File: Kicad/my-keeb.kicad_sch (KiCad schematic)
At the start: 262 parts, among them SW10 SW_Push, SW11 SW_Push, SW12 SW_Push, SW13 SW_Push, SW14 SW_Push, SW15 SW_Push, SW16 SW_Push, SW17 SW_Push, SW18 SW_Push, SW19 SW_Push, SW2 SW_Push, SW20 SW_Push, SW21 SW_Push, SW22 SW_Push, SW23 SW_Push, SW24 SW_Push, SW25 SW_Push, SW26 SW_Push, SW27 SW_Push, SW29 SW_Push, SW3 SW_Push, SW30 SW_Push, SW31 SW_Push, SW32 SW_Push, SW33 SW_Push, SW34 SW_Push, SW35 SW_Push, SW36 SW_Push, SW37 SW_Push, SW38 SW_Push, SW39 SW_Push, SW4 SW_Push, SW40 SW_Push, SW41 SW_Push, SW42 SW_Push, SW43 SW_Push, SW44 SW_Push, SW45 SW_Push, SW46 SW_Push, SW47 SW_Push, SW48 SW_Push, SW49 SW_Push, SW5 SW_Push, SW50 SW_Push, SW51 SW_Push, SW52 SW_Push, SW53 SW_Push, SW54 SW_Push, SW55 SW_Push, SW57 SW_Push, SW58 SW_Push, SW6 SW_Push, SW60 SW_Push, SW61 SW_Push, SW62 SW_Push, SW63 SW_Push, SW64 SW_Push, SW65 SW_Push, SW66 SW_Push, SW67 SW_Push, SW68 SW_Push, SW69 SW_Push, SW7 SW_Push, SW71 SW_Push, SW72 SW_Push, SW73 SW_Push, SW74 SW_Push, SW77 SW_Push, SW79 SW_Push, SW8 SW_Push, SW80 SW_Push, SW81 SW_Push, SW82 SW_Push, SW86 SW_Push, SW87 SW_Push, SW88 SW_Push, SW89 SW_Push, SW9 SW_Push, SW90 SW_Push, SW91 SW_Push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

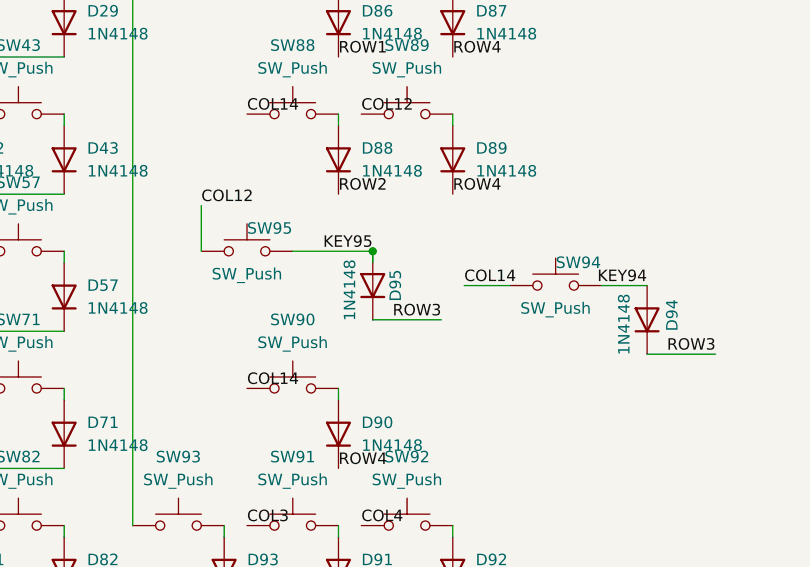
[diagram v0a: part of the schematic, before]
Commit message: Organize files into folders
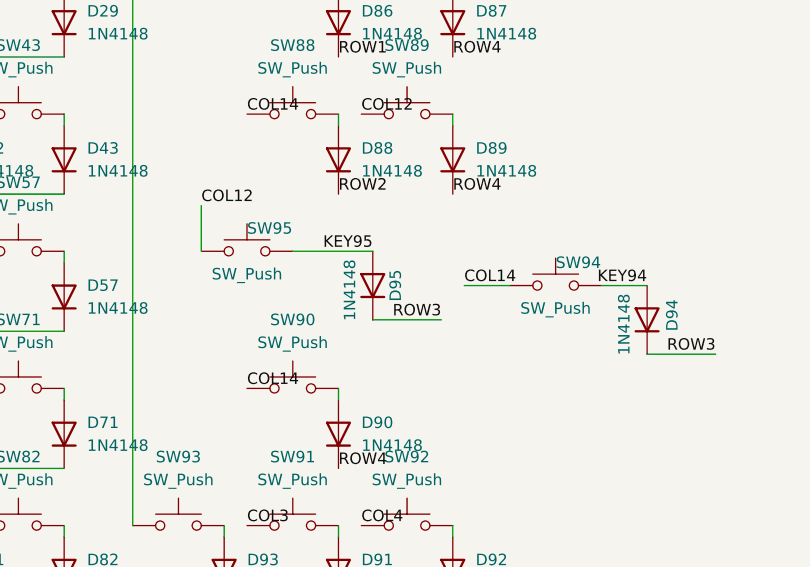
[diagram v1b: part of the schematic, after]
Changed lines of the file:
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@@
 	)
 	(junction
-		(at 243.84 68.58)
-		(diameter 0)
-		(color 0 0 0 0)
-	)
-	(junction
 		(at 44.45 77.47)
 		(diameter 0)
@@
 	(wire
 		(pts
-			(xy 251.46 76.2) (xy 243.84 76.2)
+			(xy 243.84 76.2) (xy 251.46 76.2)
 		)
 		(stroke
@@
 	(wire
 		(pts
+			(xy 243.84 68.58) (xy 234.95 68.58)
+		)
+		(stroke
+			(width 0)
+			(type default)
+		)
+	)
+	(wire
+		(pts
 			(xy 284.48 121.92) (xy 275.59 121.92)
 		)
@@
 	(wire
 		(pts
-			(xy 243.84 69.85) (xy 243.84 68.58)
-		)
-		(stroke
-			(width 0)
-			(type default)
-		)
-	)
-	(wire
-		(pts
 			(xy 224.79 -120.65) (xy 234.95 -120.65)
 		)
@@
 		)
 		(stroke
-			(width 0)
-			(type default)
-		)
-	)
-	(wire
-		(pts
-			(xy 243.84 68.58) (xy 234.95 68.58)
-		)
-		(stroke
